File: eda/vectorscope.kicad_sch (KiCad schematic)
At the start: 74 parts, among them J1 EXT PWR, J2 IO CONNECTOR, J3 SCOPE, J4 SIGGEN, P1 IO_PLUG_USB, Q1 DMG2301L, SW1 USER, SW10 MENU, SW11 LEVEL, SW12 RANGE, SW13 JOYSTICK, SW14 PWR, SW2 SAVE, SW3 SW_A, SW4 SW_B, SW5 SW_C, SW6 SW_D, SW7 XY, SW8 WAVE, SW9 SEL, U1 AK4619VN, U2 LMV324, U3 TLC59283, U4 TPA321

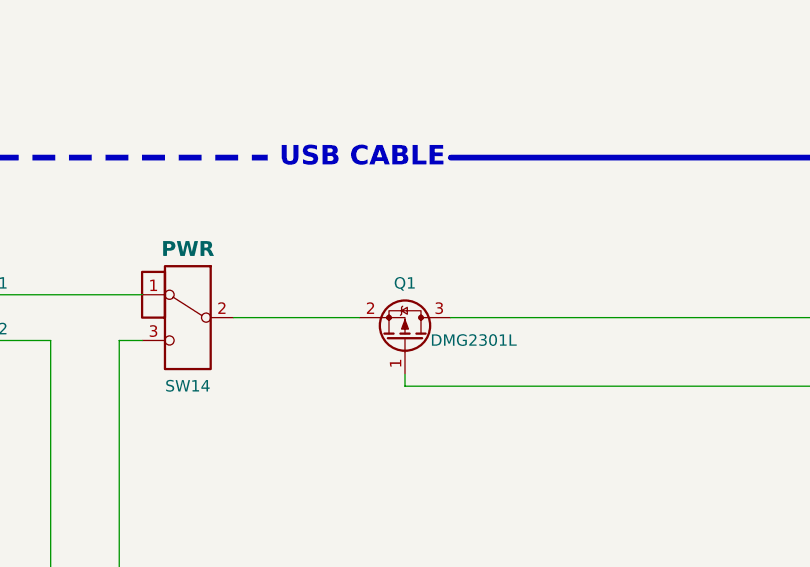
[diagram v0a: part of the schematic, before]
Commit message: cleaned up DRC schematic errors, assigned original footprints schematics
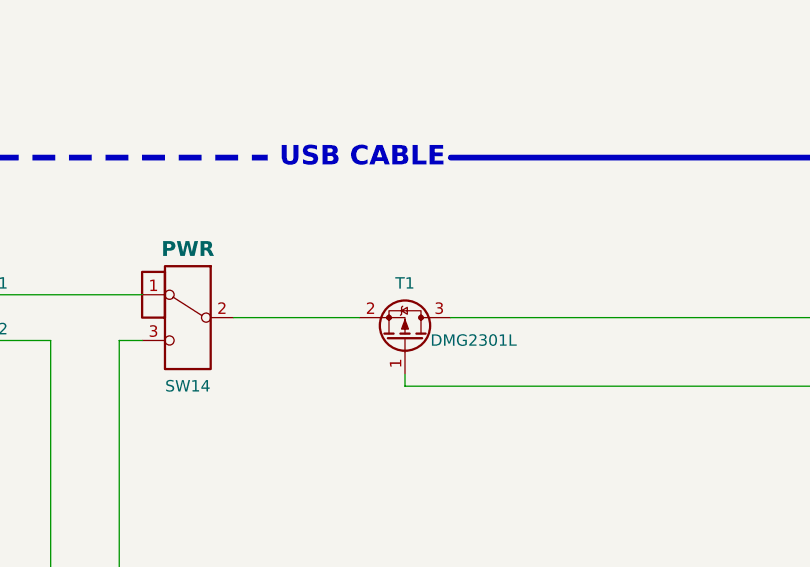
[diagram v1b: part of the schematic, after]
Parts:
- C1, C2: footprint (none) -> .vector-orig:_Users_Voja_Desktop_Projekti_Gio.PcbLib_Tantal
- C10, C11, C12, C13, C14, C15, C16, C17, C18, C19, C20, C3, C4, C5, C6, C7, C8, C9, R1, R10, R11, R12, R13, R2, R3, R4, R5, R6, R7, R8, R9, SW1: footprint (none) -> .vector-orig:_Users_Voja_Desktop_CUBE_ESP.PcbLib_TANTALUM KEMET C
- L1: footprint (none) -> .vector-orig:0805
- LY1, LY2, LY3, LY4, LY5, LY6, LY7, LY8: footprint (none) -> .vector-orig:_Users_Voja_Desktop_ESP.PcbLib_LED0603
- SW10, SW11, SW12: footprint (none) -> .vector-orig:key 12x12 SMD
- SW13: footprint (none) -> .vector-orig:_Users_Voja_Desktop_Projekti_Gio.PcbLib_JOYSTICK 2
- SW2, SW3, SW4, SW5, SW6, SW7, SW8, SW9: footprint (none) -> .vector-orig:_Users_Voja_Documents_GitHub_willo-pcb_ESP.PcbLib_key4p
- T1: renamed from Q1; footprint Package_TO_SOT_SMD:SOT-23 -> .vector-orig:SOT-23
- TP1, TP2: footprint (none) -> .vector:TestPoint_Pad_200_140_mils
- U1: footprint Package_DFN_QFN:QFN-32-1EP_5x5mm_P0.5mm_EP3.6x3.6mm -> .vector-orig:AK4619
- U2: footprint (none) -> .vector-orig:TSSOP 14
- U4: footprint (none) -> .vector-orig:_Users_Voja_Desktop_CUBE_ESP.PcbLib_MSOP8
- XM1: footprint Raspberry Pi:MODULE_SC0918 -> .vector-orig:_Users_Voja_Desktop_Projekti_Gio.PcbLib_PICO
- ZD1: footprint (none) -> .vector-orig:SOT-23
